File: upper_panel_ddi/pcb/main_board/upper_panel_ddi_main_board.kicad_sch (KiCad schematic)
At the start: 3 parts, among them J1 ROW0-7, J2 COL0-4

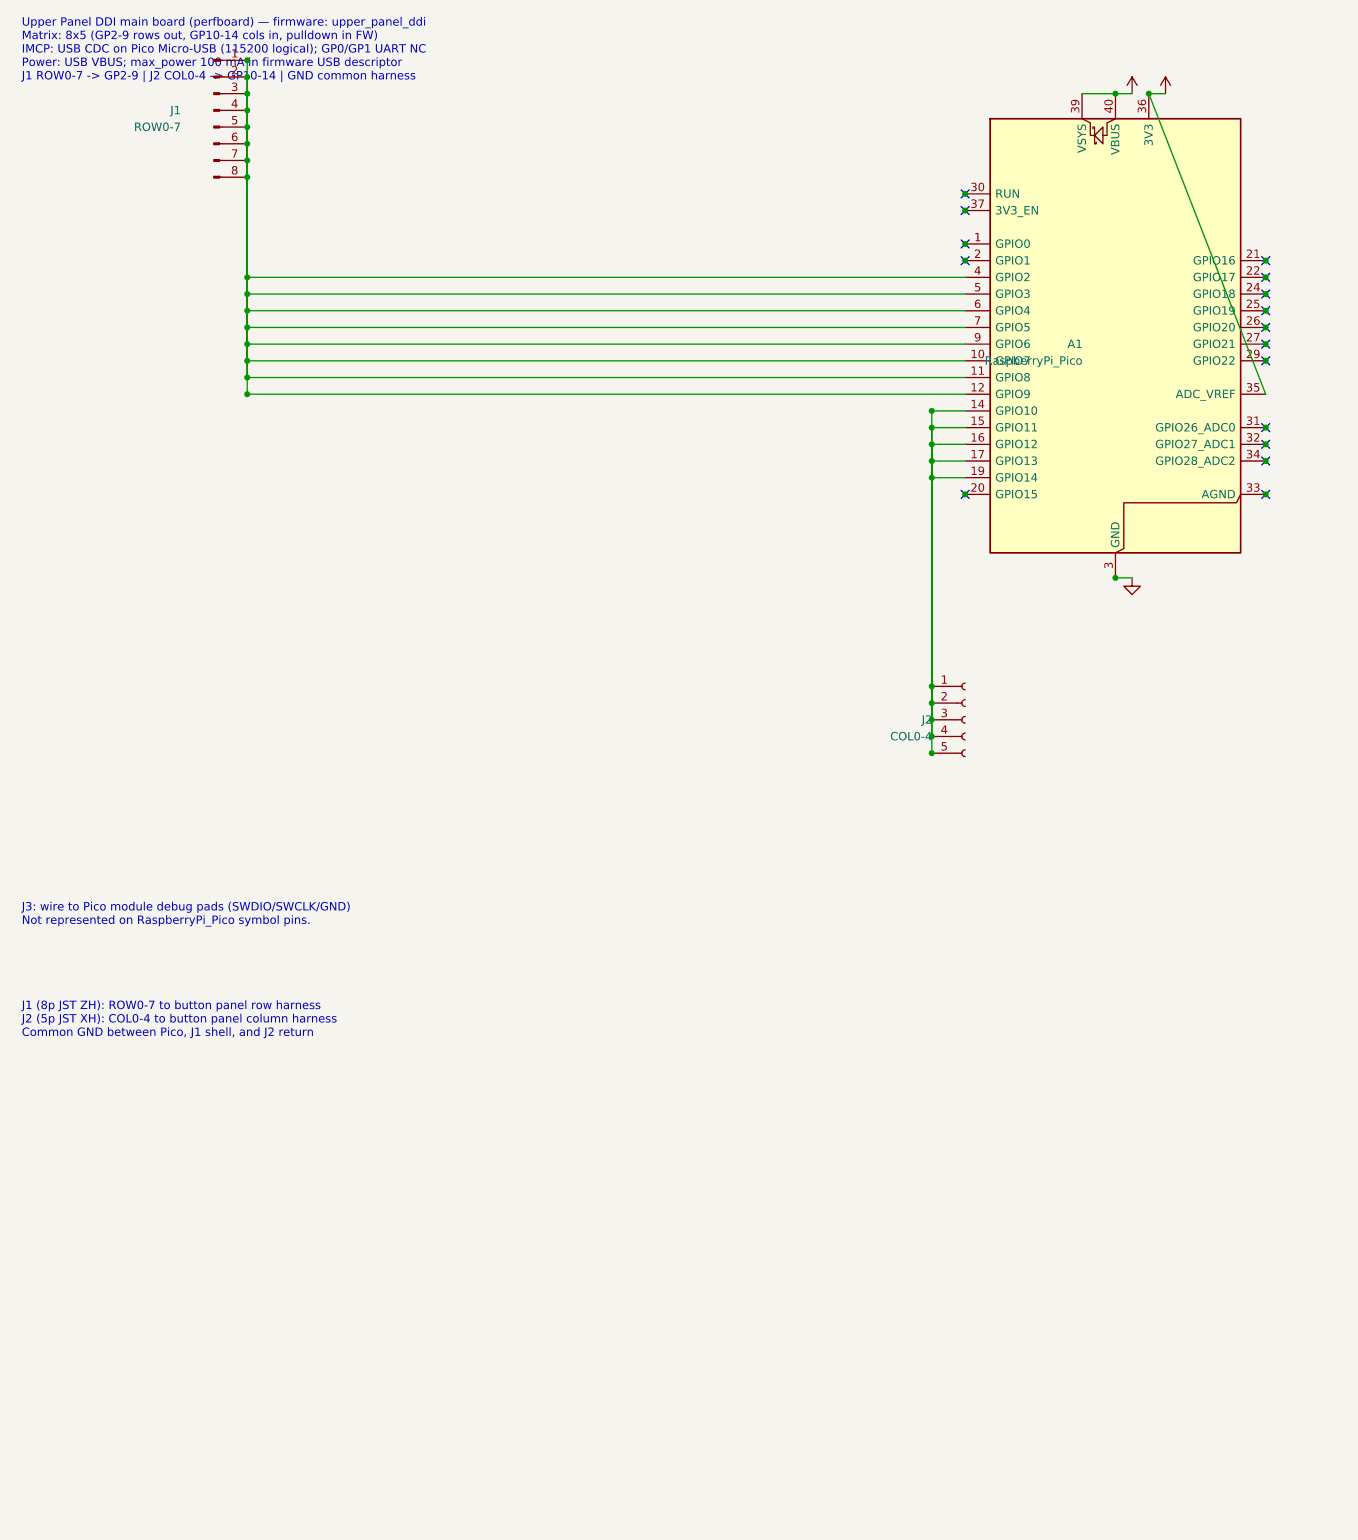
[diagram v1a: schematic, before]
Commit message: fix(hardware): align main_board with eight button_panel 1x08 harnesses
Replace centralized row/column connectors with J1..J8 socket pinout
matching button_panel J1, use global labels for readable matrix wiring,
and embed Conn_01x08_Socket for schematic generation.

Co-authored-by: Cursor <cursoragent@cursor.com>
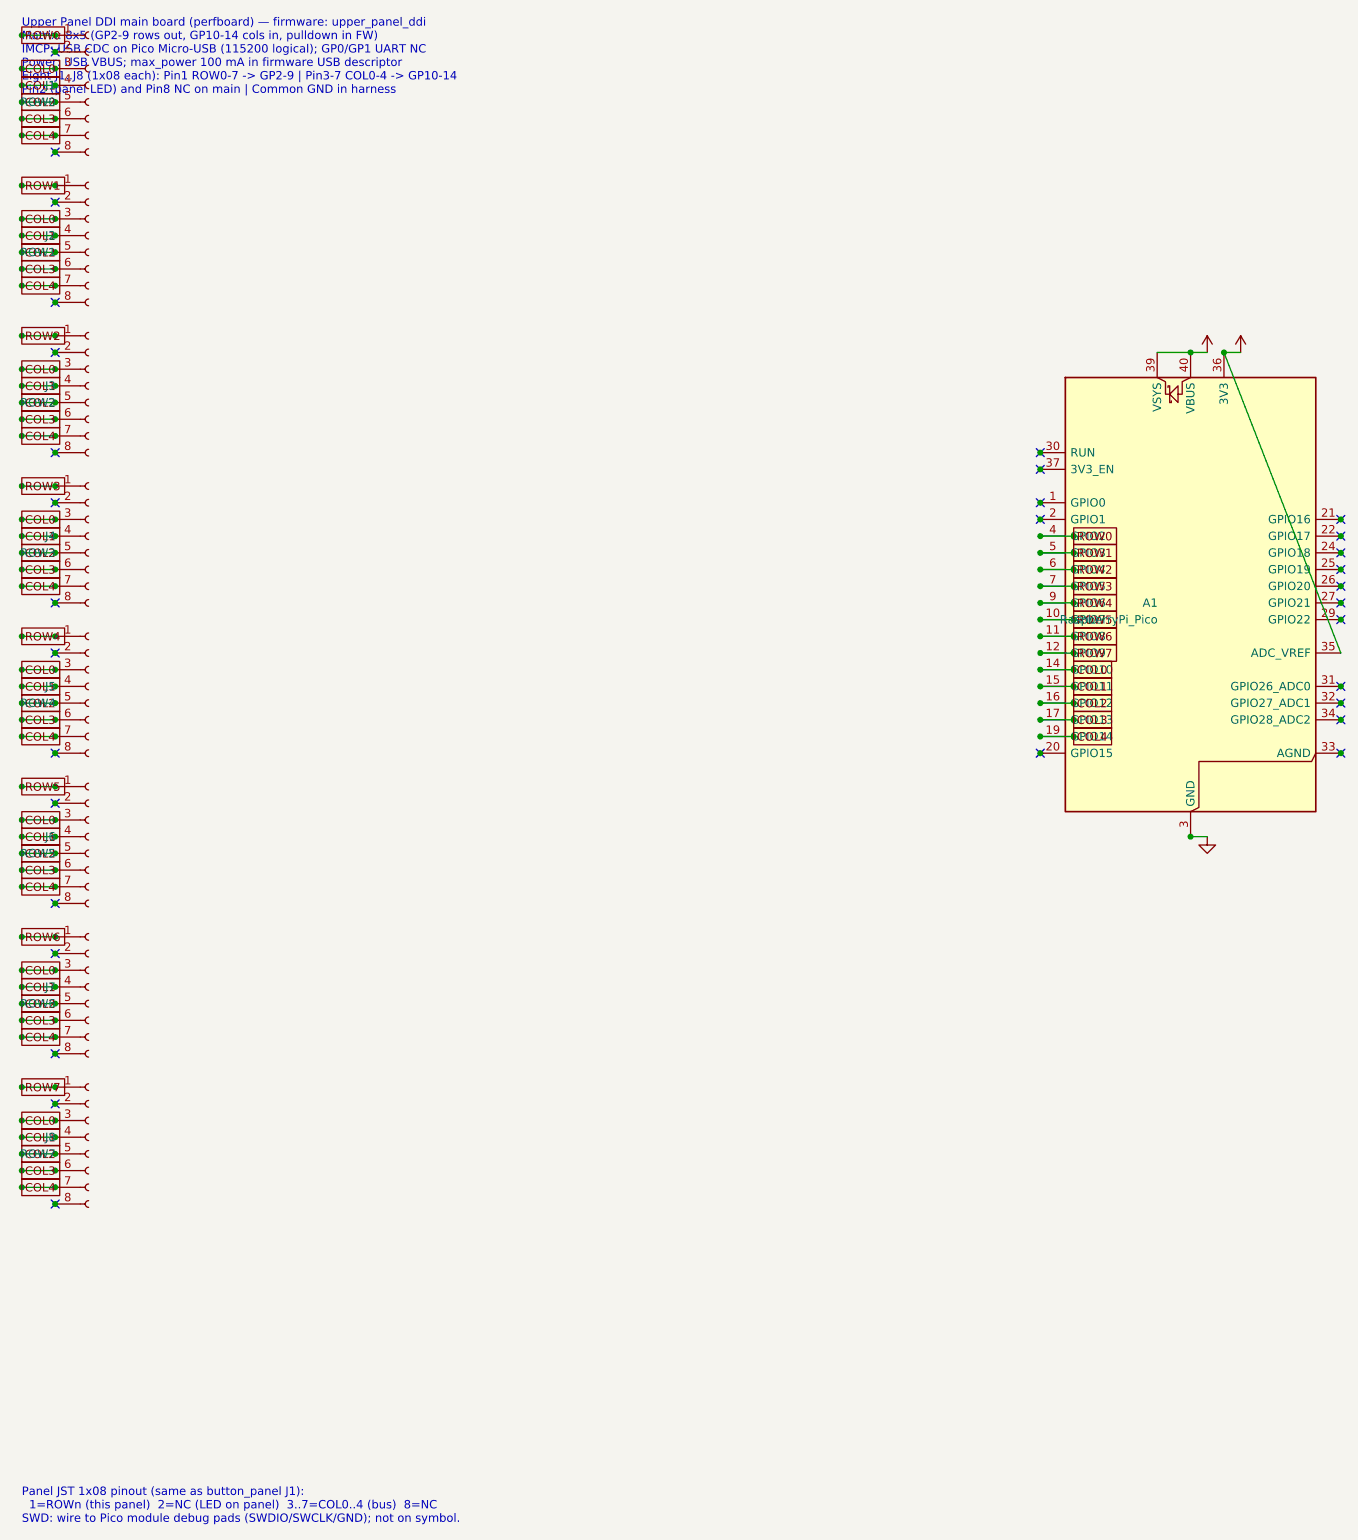
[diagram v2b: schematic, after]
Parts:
- removed J2: COL0-4, Connector_JST:JST_XH_B5B-XH-AM_1x05_P2.50mm_Vertical, symbol Connector:Conn_01x05_Socket
- added J2: ROW1, Connector_JST:JST_ZH_B8B-ZR_1x08_P1.50mm_Vertical, symbol Connector:Conn_01x08_Socket
- added J3: ROW2, Connector_JST:JST_ZH_B8B-ZR_1x08_P1.50mm_Vertical, symbol Connector:Conn_01x08_Socket
- added J4: ROW3, Connector_JST:JST_ZH_B8B-ZR_1x08_P1.50mm_Vertical, symbol Connector:Conn_01x08_Socket
- added J5: ROW4, Connector_JST:JST_ZH_B8B-ZR_1x08_P1.50mm_Vertical, symbol Connector:Conn_01x08_Socket
- added J6: ROW5, Connector_JST:JST_ZH_B8B-ZR_1x08_P1.50mm_Vertical, symbol Connector:Conn_01x08_Socket
- added J7: ROW6, Connector_JST:JST_ZH_B8B-ZR_1x08_P1.50mm_Vertical, symbol Connector:Conn_01x08_Socket
- added J8: ROW7, Connector_JST:JST_ZH_B8B-ZR_1x08_P1.50mm_Vertical, symbol Connector:Conn_01x08_Socket
- J1: value ROW0-7 -> ROW0; symbol Connector:Conn_01x08_Pin -> Connector:Conn_01x08_Socket
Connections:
- new net COL0: A1.14 (GPIO10), J1.3 (Pin_3), J2.3 (Pin_3), J3.3 (Pin_3), J4.3 (Pin_3), J5.3 (Pin_3), J6.3 (Pin_3), J7.3 (Pin_3), J8.3 (Pin_3)
- new net COL1: A1.15 (GPIO11), J1.4 (Pin_4), J2.4 (Pin_4), J3.4 (Pin_4), J4.4 (Pin_4), J5.4 (Pin_4), J6.4 (Pin_4), J7.4 (Pin_4), J8.4 (Pin_4)
- new net COL2: A1.16 (GPIO12), J1.5 (Pin_5), J2.5 (Pin_5), J3.5 (Pin_5), J4.5 (Pin_5), J5.5 (Pin_5), J6.5 (Pin_5), J7.5 (Pin_5), J8.5 (Pin_5)
- new net COL3: A1.17 (GPIO13), J1.6 (Pin_6), J2.6 (Pin_6), J3.6 (Pin_6), J4.6 (Pin_6), J5.6 (Pin_6), J6.6 (Pin_6), J7.6 (Pin_6), J8.6 (Pin_6)
- new net COL4: A1.19 (GPIO14), J1.7 (Pin_7), J2.7 (Pin_7), J3.7 (Pin_7), J4.7 (Pin_7), J5.7 (Pin_7), J6.7 (Pin_7), J7.7 (Pin_7), J8.7 (Pin_7)
- new net ROW0: A1.4 (GPIO2), J1.1 (Pin_1)
- new net ROW1: A1.5 (GPIO3), J2.1 (Pin_1)
- new net ROW2: A1.6 (GPIO4), J3.1 (Pin_1)
- new net ROW3: A1.7 (GPIO5), J4.1 (Pin_1)
- new net ROW4: A1.9 (GPIO6), J5.1 (Pin_1)
- new net ROW5: A1.10 (GPIO7), J6.1 (Pin_1)
- new net ROW6: A1.11 (GPIO8), J7.1 (Pin_1)
- new net ROW7: A1.12 (GPIO9), J8.1 (Pin_1)
- now unconnected: J1.2 (Pin_2), J1.8 (Pin_8)
- no-connect marks 16 -> 32
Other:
- note added: "Panel JST 1x08 pinout (same as button_panel J1): 1=ROWn (this panel) 2=NC (LED on panel) 3..7=COL0..4 (bus) 8=NC SWD: wire to Pico module debug pads (SWDIO/SWCLK/GND); not on symbol."
- note added: "Upper Panel DDI main board (perfboard) — firmware: upper_panel_ddi Matrix: 8x5 (GP2-9 rows out, GP10-14 cols in, pulldown in FW) IMCP: USB CDC on Pico Micro-USB (115200 logical); GP0/GP1 UART NC Power: USB VBUS; max_power 100 mA in firmware USB descriptor Eight J1..J8 (1x08 each): Pin1 ROW0-7 -> GP2-9 | Pin3-7 COL0-4 -> GP10-14 Pin2 (panel LED) and Pin8 NC on main | Common GND in harness"
- note removed: "J1 (8p JST ZH): ROW0-7 to button panel row harness J2 (5p JST XH): COL0-4 to button panel column harness Common GND between Pico, J1 shell, and J2 return"
- note removed: "J3: wire to Pico module debug pads (SWDIO/SWCLK/GND) Not represented on RaspberryPi_Pico symbol pins."
- note removed: "Upper Panel DDI main board (perfboard) — firmware: upper_panel_ddi Matrix: 8x5 (GP2-9 rows out, GP10-14 cols in, pulldown in FW) IMCP: USB CDC on Pico Micro-USB (115200 logical); GP0/GP1 UART NC Power: USB VBUS; max_power 100 mA in firmware USB descriptor J1 ROW0-7 -> GP2-9 | J2 COL0-4 -> GP10-14 | GND common harness"
- moved on the sheet: A1
